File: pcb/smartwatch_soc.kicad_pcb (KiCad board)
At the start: 4 copper layers, 45.6 x 31 mm, 31 parts, among them J2 USB_B_Micro, SW1 CK_KMS2xxGP, SW2 Button, SW3 Button, SW4 Button, SW5 Button, SW7 CK_KMS2xxGP, U1 MIC5219-3.3YM5, U2 LSM6DS3, U3 OLED_Display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

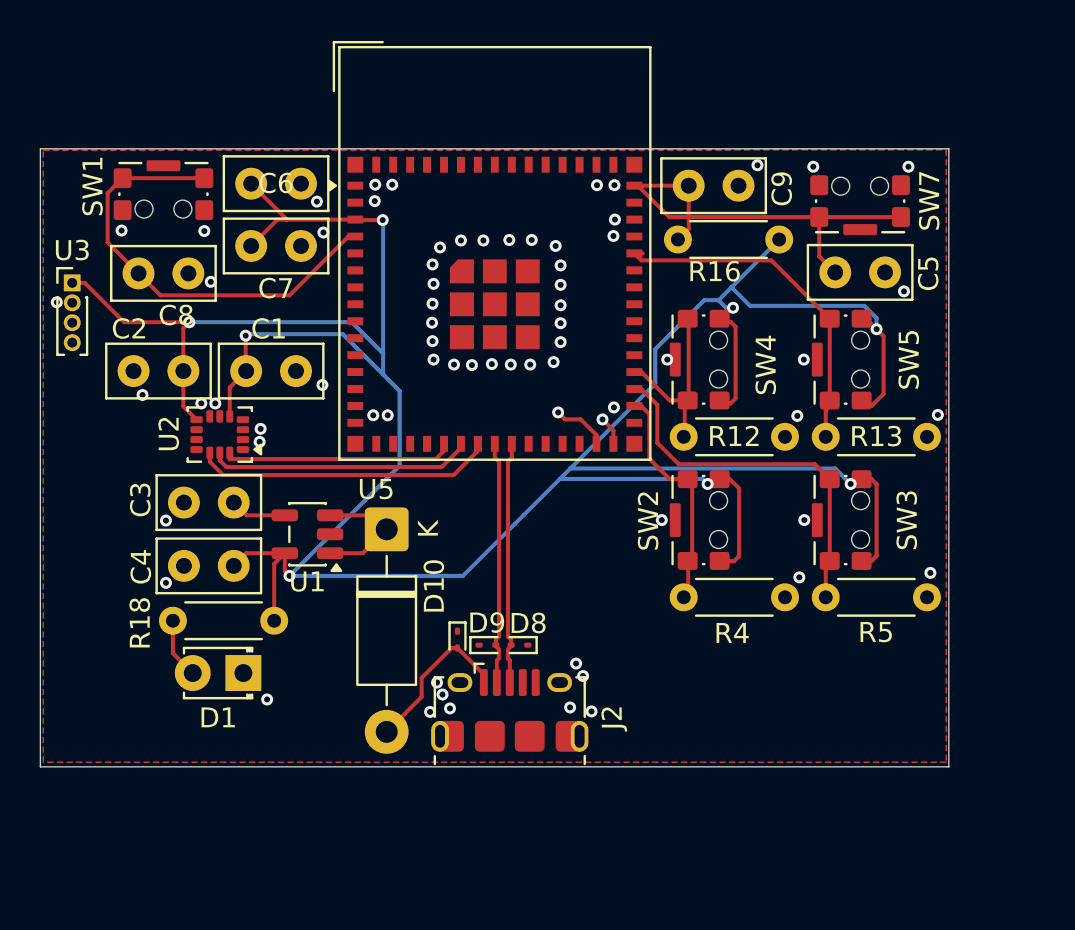
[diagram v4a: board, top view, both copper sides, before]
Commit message: added labels
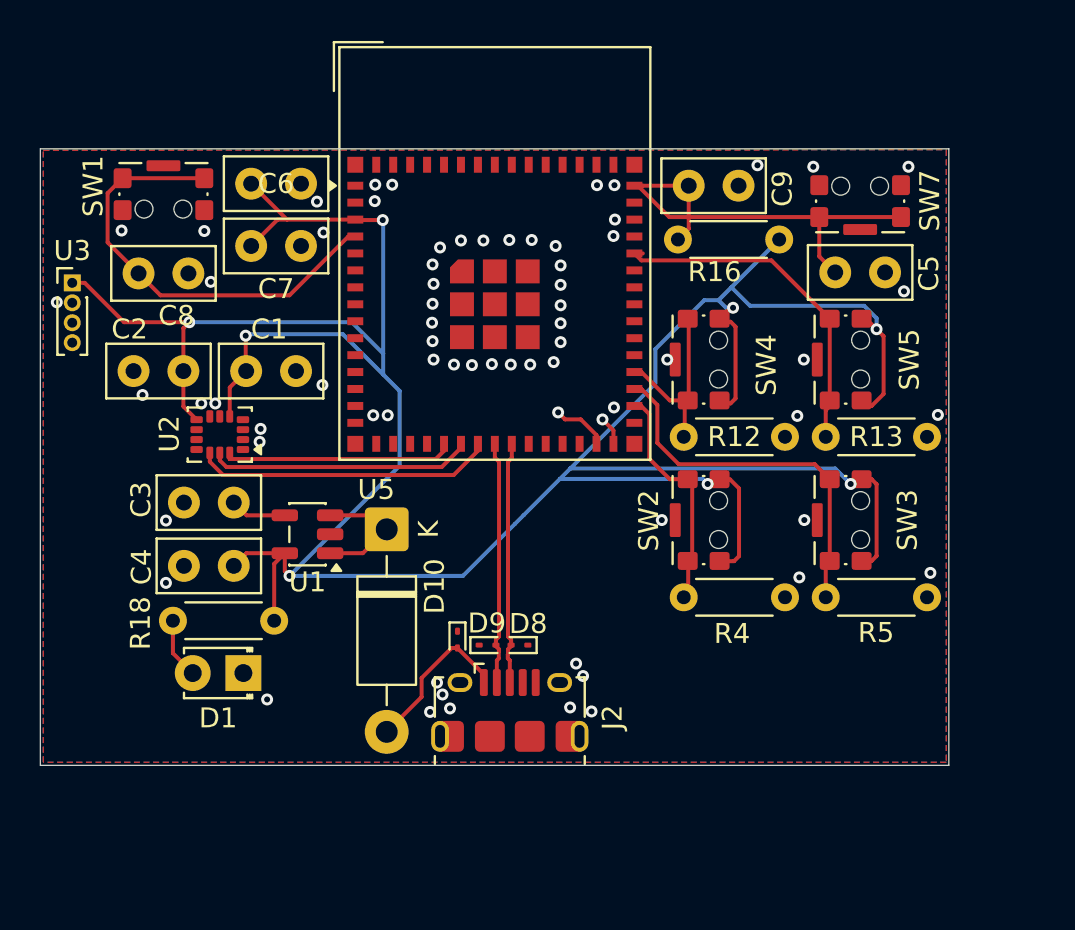
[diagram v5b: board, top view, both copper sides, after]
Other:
- board size 45.6 x 31 mm -> 45.6 x 30.9 mm
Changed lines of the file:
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@@
 	(gr_rect
 		(start 138.5 60.925)
-		(end 184.075 91.93)
+		(end 184.075 91.855)
 		(stroke
 			(width 0.05)
@@
 		(min_thickness 0.1524)
 		(filled_areas_thickness no)
-		(fill yes
+		(fill
 			(thermal_gap 0.5)
 			(thermal_bridge_width 0.5)
